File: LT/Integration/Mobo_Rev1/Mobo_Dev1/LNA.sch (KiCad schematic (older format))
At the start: 8 parts, among them J5 Conn_01x02_Male, J6 Conn_Coaxial, Q1 2N5486

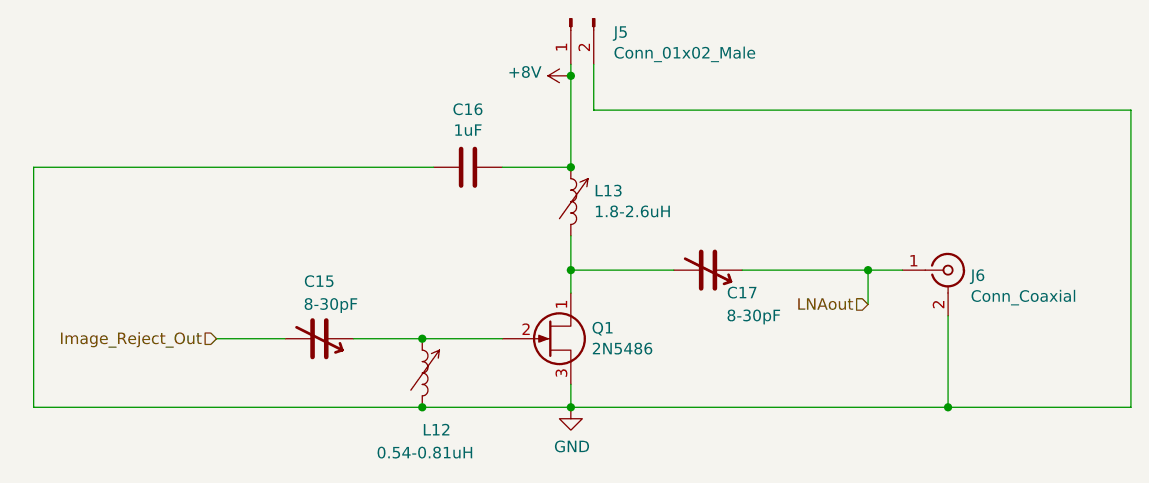
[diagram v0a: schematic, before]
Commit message: Added the preliminary layout for the Phase 2 motherboard, not at all finished yet
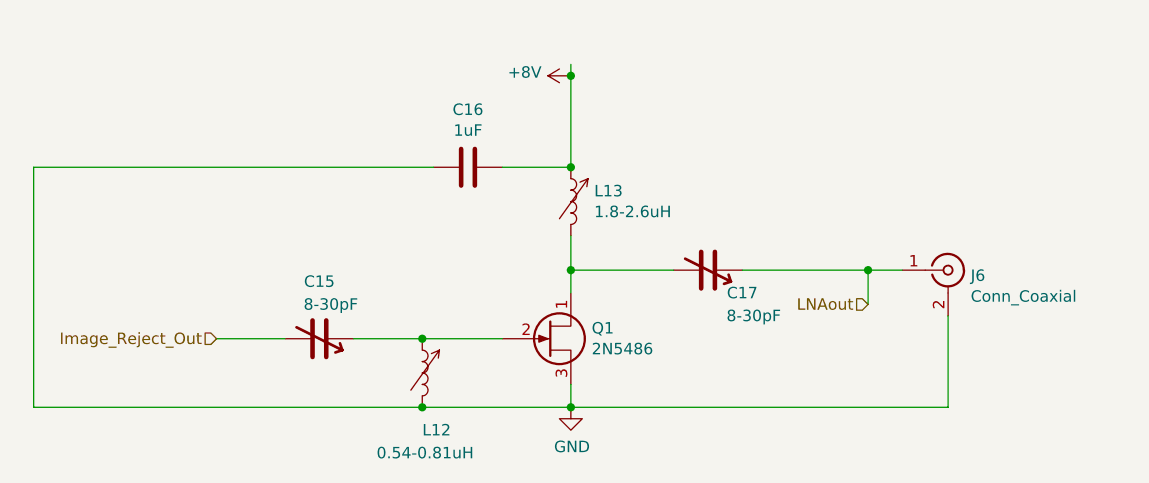
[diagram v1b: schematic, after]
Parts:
- removed J5: Conn_01x02_Male, Connector_PinHeader_2.54mm:PinHeader_1x02_P2.54mm_Vertical, symbol Connector:Conn_01x02_Male
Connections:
- wire segments 23 -> 19
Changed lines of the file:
@@
 	3500 1900 3500 2050
 Connection ~ 3500 2050
-$Comp
-L Connector:Conn_01x02_Male J5
-U 1 1 5E4711B0
-P 3500 950
-F 0 "J5" V 3560 763 50  0000 R CNN
-F 1 "Conn_01x02_Male" V 3651 763 50  0000 R CNN
-F 2 "Connector_PinHeader_2.54mm:PinHeader_1x02_P2.54mm_Vertical" H 3500 950 50  0001 C CNN
-F 3 "~" H 3500 950 50  0001 C CNN
-	1    3500 950
-	0    -1   1    0
-$EndComp
 Wire Wire Line
 	3500 1150 3500 1200
-Wire Wire Line
-	3600 1150 3600 1350
-Wire Wire Line
-	3600 1350 5950 1350
 Wire Wire Line
 	2850 2650 3500 2650
@@
 Wire Wire Line
 	1150 1600 1150 2650
-Wire Wire Line
-	5950 1350 5950 2650
 $Comp
 L power:GND #PWR012
@@
 	4800 2050 4950 2050
 Wire Wire Line
-	5150 2650 5950 2650
-Wire Wire Line
 	3500 2650 5150 2650
-Connection ~ 5150 2650
 Wire Wire Line
 	5150 2250 5150 2650
